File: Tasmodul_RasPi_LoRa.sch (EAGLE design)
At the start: 59 parts, among them J1 691322310002, J2 RASPI_4B, J3 LORA_MPCIE, J4 636101111001, J5 60311002111526, J6 60311002111526, Q1 DMN3404L-7, U1 AP64351, U2 QUECTEL_L76-M33, U3 REG1117

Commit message: * Added more description to the schematic * Added more silk screen information to the PCB * Added U.fl connectors for the SMA connectors as a backup
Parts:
- added J7, J8: 60311002111526, Wurth_Connectors_WR-SMA:60311002111526
- C17, C21: value (none) -> dnp
- J5, J6: value 60311002111526 -> 636101111001; device Wurth_Connectors_WR-SMA:60311002111526 -> Wurth_Connectors_WR-UMRF:636101111001
- R10: value (none) -> 10R
- R11: value (none) -> 0R
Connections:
- new net HF_GNSS: J6.1, J8.1
- new net HF_LORA: J5.1, J7.1
- net GND: now also J7.2, J8.2
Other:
- note added: "GNSS"
- note added: "LoRa"
- note added: "SMA -> U.fl"
- moved on the sheet: J5, J6
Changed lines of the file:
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@@
 <part name="GND20" library="supply1" deviceset="GND" device=""/>
 <part name="L2" library="Wurth_EMC Components_WE-CBF" library_urn="urn:adsk.eagle:library:14283147" deviceset="WE-CBF_0603" device="_WB_HS" package3d_urn="urn:adsk.eagle:package:7784393/8" technology="_74279262" value="120ohm@100 MHz"/>
-<part name="R10" library="rcl" library_urn="urn:adsk.eagle:library:334" deviceset="R-EU_" device="R0603" package3d_urn="urn:adsk.eagle:package:23555/3"/>
+<part name="R10" library="rcl" library_urn="urn:adsk.eagle:library:334" deviceset="R-EU_" device="R0603" package3d_urn="urn:adsk.eagle:package:23555/3" value="10R"/>
 <part name="JMP1" library="jump-0r-smd" library_urn="urn:adsk.eagle:library:251" deviceset="0R-JUMP" device="A" package3d_urn="urn:adsk.eagle:package:15385/1"/>
 <part name="JMP2" library="jump-0r-smd" library_urn="urn:adsk.eagle:library:251" deviceset="0R-JUMP" device="A" package3d_urn="urn:adsk.eagle:package:15385/1"/>
@@
 <part name="D2" library="diode" library_urn="urn:adsk.eagle:library:210" deviceset="DIODE-" device="SOD323-R" package3d_urn="urn:adsk.eagle:package:43437/1" value="CUS551V30,H3F"/>
 <part name="GND22" library="supply1" deviceset="GND" device=""/>
-<part name="J5" library="Wurth_Connectors_WR-SMA" library_urn="urn:adsk.eagle:library:15011170" deviceset="60311002111526" device="" package3d_urn="urn:adsk.eagle:package:15011192/3" value="60311002111526"/>
-<part name="J6" library="Wurth_Connectors_WR-SMA" library_urn="urn:adsk.eagle:library:15011170" deviceset="60311002111526" device="" package3d_urn="urn:adsk.eagle:package:15011192/3" value="60311002111526"/>
-<part name="C17" library="rcl" library_urn="urn:adsk.eagle:library:334" deviceset="C-EU" device="C0603" package3d_urn="urn:adsk.eagle:package:23616/2"/>
-<part name="R11" library="rcl" library_urn="urn:adsk.eagle:library:334" deviceset="R-EU_" device="R0603" package3d_urn="urn:adsk.eagle:package:23555/3"/>
-<part name="C21" library="rcl" library_urn="urn:adsk.eagle:library:334" deviceset="C-EU" device="C0603" package3d_urn="urn:adsk.eagle:package:23616/2"/>
+<part name="J7" library="Wurth_Connectors_WR-SMA" library_urn="urn:adsk.eagle:library:15011170" deviceset="60311002111526" device="" package3d_urn="urn:adsk.eagle:package:15011192/3" value="60311002111526"/>
+<part name="J8" library="Wurth_Connectors_WR-SMA" library_urn="urn:adsk.eagle:library:15011170" deviceset="60311002111526" device="" package3d_urn="urn:adsk.eagle:package:15011192/3" value="60311002111526"/>
+<part name="C17" library="rcl" library_urn="urn:adsk.eagle:library:334" deviceset="C-EU" device="C0603" package3d_urn="urn:adsk.eagle:package:23616/2" value="dnp"/>
+<part name="R11" library="rcl" library_urn="urn:adsk.eagle:library:334" deviceset="R-EU_" device="R0603" package3d_urn="urn:adsk.eagle:package:23555/3" value="0R"/>
+<part name="C21" library="rcl" library_urn="urn:adsk.eagle:library:334" deviceset="C-EU" device="C0603" package3d_urn="urn:adsk.eagle:package:23616/2" value="dnp"/>
+<part name="J5" library="Wurth_Connectors_WR-UMRF" library_urn="urn:adsk.eagle:library:27699748" deviceset="636101111001" device="" package3d_urn="urn:adsk.eagle:package:27699753/5" value="636101111001"/>
+<part name="J6" library="Wurth_Connectors_WR-UMRF" library_urn="urn:adsk.eagle:library:27699748" deviceset="636101111001" device="" package3d_urn="urn:adsk.eagle:package:27699753/5" value="636101111001"/>
 </parts>
 <sheets>
@@
 https://forum.openwrt.org/t/official-raspberry-pi-4-fan-yes-instructions-inside/93975</text>
 <text x="40.64" y="116.84" size="1.778" layer="91" rot="R180">Place only one</text>
+<text x="363.22" y="116.84" size="1.778" layer="91">LoRa</text>
+<text x="363.22" y="101.6" size="1.778" layer="91">GNSS</text>
+<text x="350.52" y="129.54" size="1.778" layer="91" align="center">SMA -&gt; U.fl</text>
 </plain>
 <instances>
@@
 <attribute name="VALUE" x="273.304" y="216.281" size="1.778" layer="96"/>
 </instance>
-<instance part="GND16" gate="1" x="284.48" y="134.62" smashed="yes">
-<attribute name="VALUE" x="281.94" y="132.08" size="1.778" layer="96"/>
+<instance part="GND16" gate="1" x="350.52" y="96.52" smashed="yes">
+<attribute name="VALUE" x="347.98" y="93.98" size="1.778" layer="96"/>
 </instance>
 <instance part="R4" gate="G$1" x="50.8" y="114.3" smashed="yes" rot="MR0">
@@
 <attribute name="VALUE" x="22.86" y="20.32" size="1.778" layer="96"/>
 </instance>
-<instance part="J5" gate="G$1" x="294.64" y="160.02" smashed="yes" rot="MR0">
-<attribute name="NAME" x="294.64" y="163.576" size="1.778" layer="95" rot="MR0" align="bottom-center"/>
-</instance>
-<instance part="J6" gate="G$1" x="294.64" y="144.78" smashed="yes" rot="MR0">
-<attribute name="NAME" x="294.64" y="148.336" size="1.778" layer="95" rot="MR0" align="bottom-center"/>
+<instance part="J7" gate="G$1" x="360.68" y="121.92" smashed="yes" rot="MR0">
+<attribute name="NAME" x="360.68" y="125.476" size="1.778" layer="95" rot="MR0" align="bottom-center"/>
+</instance>
+<instance part="J8" gate="G$1" x="360.68" y="106.68" smashed="yes" rot="MR0">
+<attribute name="NAME" x="360.68" y="110.236" size="1.778" layer="95" rot="MR0" align="bottom-center"/>
 </instance>
 <instance part="C17" gate="G$1" x="228.6" y="66.04" smashed="yes" rot="R180">
@@
 <attribute name="NAME" x="242.316" y="65.659" size="1.778" layer="95" rot="R180"/>
 <attribute name="VALUE" x="242.316" y="70.739" size="1.778" layer="96" rot="R180"/>
+</instance>
+<instance part="J5" gate="G$1" x="337.82" y="121.92" smashed="yes">
+<attribute name="NAME" x="337.82" y="125.476" size="1.778" layer="95" align="bottom-center"/>
+<attribute name="VALUE" x="337.82" y="114.3" size="1.778" layer="96" align="bottom-center"/>
+</instance>
+<instance part="J6" gate="G$1" x="337.82" y="106.68" smashed="yes">
+<attribute name="NAME" x="337.82" y="110.236" size="1.778" layer="95" align="bottom-center"/>
+<attribute name="VALUE" x="337.82" y="99.06" size="1.778" layer="96" align="bottom-center"/>
 </instance>
 </instances>
@@
 </segment>
 <segment>
+<pinref part="J7" gate="G$1" pin="2"/>
+<pinref part="GND16" gate="1" pin="GND"/>
+<wire x1="353.06" y1="116.84" x2="350.52" y2="116.84" width="0.1524" layer="91"/>
+<wire x1="350.52" y1="116.84" x2="350.52" y2="101.6" width="0.1524" layer="91"/>
+<pinref part="J8" gate="G$1" pin="2"/>
+<wire x1="350.52" y1="101.6" x2="350.52" y2="99.06" width="0.1524" layer="91"/>
+<wire x1="353.06" y1="101.6" x2="350.52" y2="101.6" width="0.1524" layer="91"/>
+<junction x="350.52" y="101.6"/>
 <pinref part="J5" gate="G$1" pin="2"/>
-<pinref part="GND16" gate="1" pin="GND"/>
-<wire x1="287.02" y1="154.94" x2="284.48" y2="154.94" width="0.1524" layer="91"/>
-<wire x1="284.48" y1="154.94" x2="284.48" y2="139.7" width="0.1524" layer="91"/>
+<wire x1="345.44" y1="116.84" x2="350.52" y2="116.84" width="0.1524" layer="91"/>
+<junction x="350.52" y="116.84"/>
 <pinref part="J6" gate="G$1" pin="2"/>
-<wire x1="284.48" y1="139.7" x2="284.48" y2="137.16" width="0.1524" layer="91"/>
-<wire x1="287.02" y1="139.7" x2="284.48" y2="139.7" width="0.1524" layer="91"/>
-<junction x="284.48" y="139.7"/>
+<wire x1="345.44" y1="101.6" x2="350.52" y2="101.6" width="0.1524" layer="91"/>
 </segment>
 <segment>
@@
 </segment>
 </net>
+<net name="HF_LORA" class="1">
+<segment>
+<pinref part="J5" gate="G$1" pin="1"/>
+<pinref part="J7" gate="G$1" pin="1"/>
+<wire x1="345.44" y1="121.92" x2="353.06" y2="121.92" width="0.1524" layer="91"/>
+</segment>
+</net>
+<net name="HF_GNSS" class="1">
+<segment>
+<pinref part="J6" gate="G$1" pin="1"/>
+<pinref part="J8" gate="G$1" pin="1"/>
+<wire x1="345.44" y1="106.68" x2="353.06" y2="106.68" width="0.1524" layer="91"/>
+</segment>
+</net>

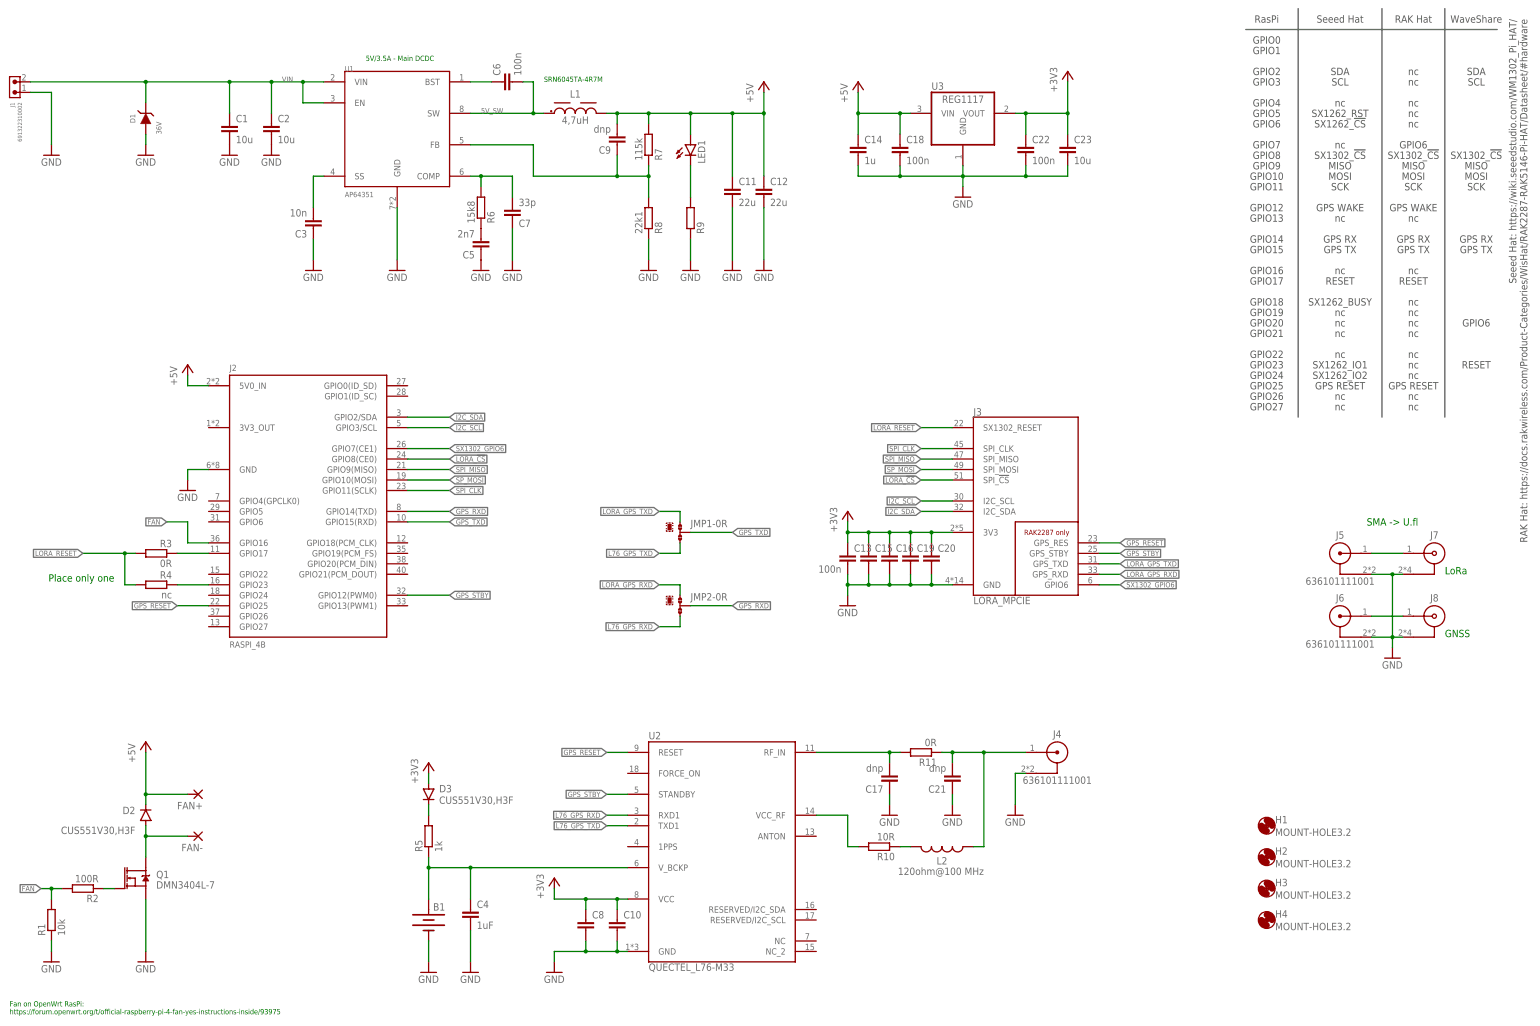
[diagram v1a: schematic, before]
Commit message: * Added multifuse to power input * Added I2C pullup resistors * Added test points to unused GPS module pins * Updated README.md
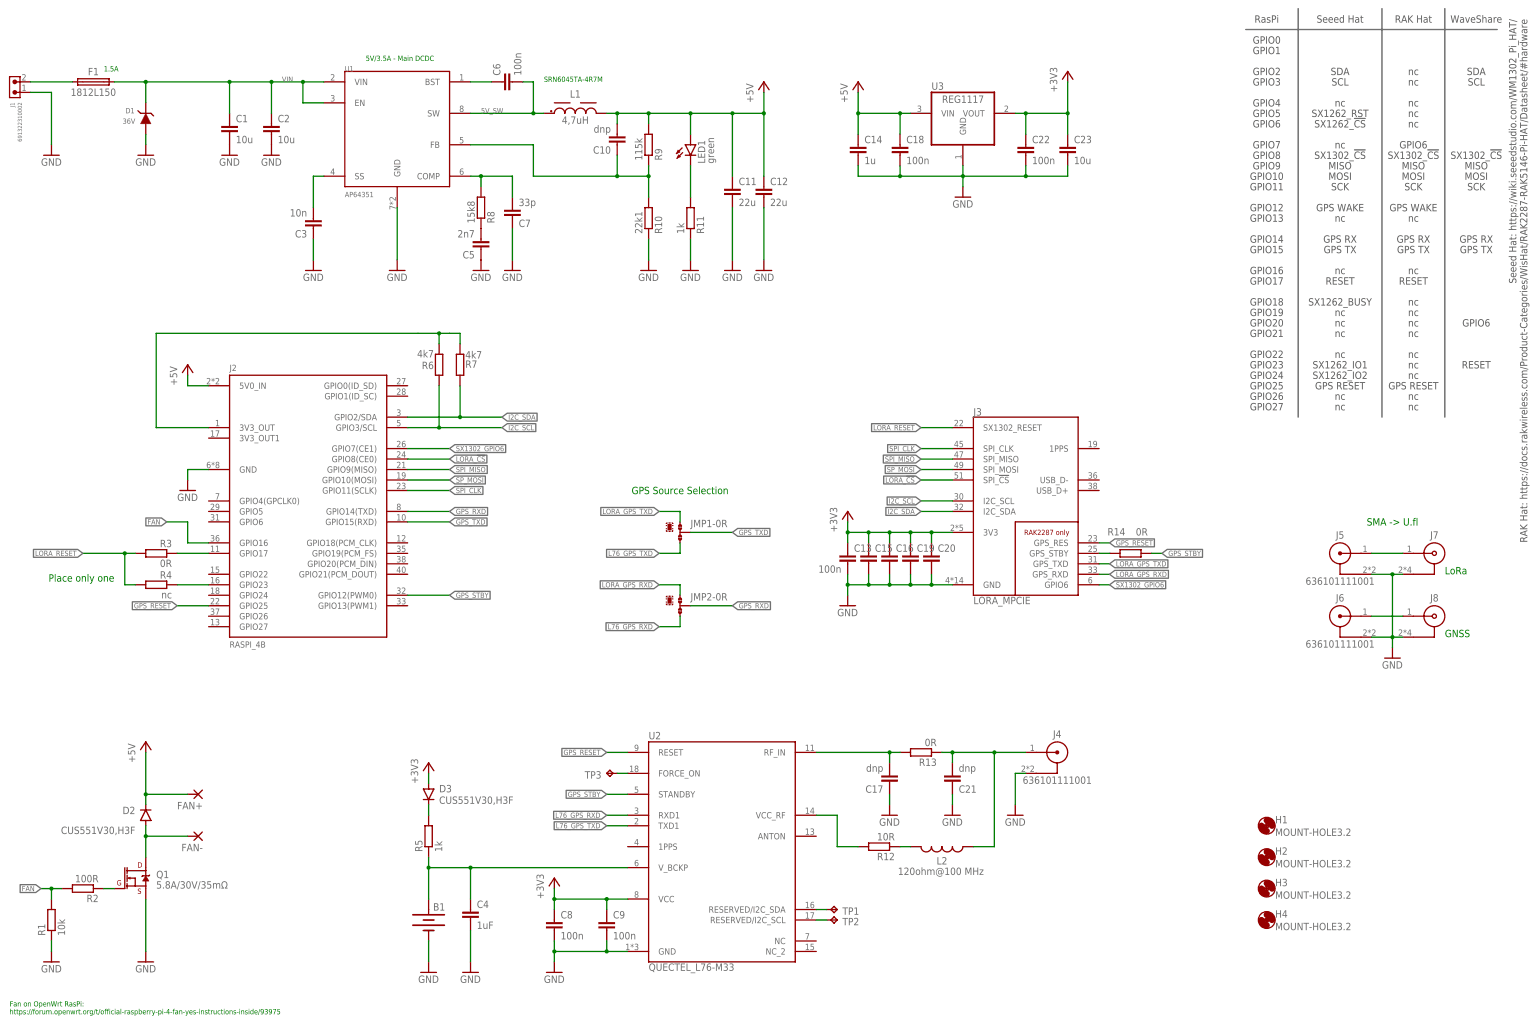
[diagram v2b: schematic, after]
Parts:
- added F1: 1812L150, Fuse:1812L150
- added R12: 10R, rcl:R-EU_R0603
- added R13, R14: 0R, rcl:R-EU_R0603
- added TP1, TP2, TP3: TPTP15R, testpad:TPTP15R
- C10: value (none) -> dnp
- C15, C16, C19, C20, C8: value (none) -> 100n
- C9: value dnp -> 100n
- LED1: value (none) -> green
- Q1: value DMN3404L-7 -> 5.8A/30V/35mΩ
- R10: value 10R -> 22k1
- R11: value 0R -> 1k
- R6: value 15k8 -> 4k7
- R7: value 115k -> 4k7
- R8: value 22k1 -> 15k8
- R9: value (none) -> 115k
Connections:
- new net N$13: J2.3V3_OUT, R6.2, R7.2
- new net N$15: F1.1, J1.2
- new net N$16: TP1.TP, U2.RESERVED/I2C_SDA
- new net N$17: TP2.TP, U2.RESERVED/I2C_SCL
- new net N$18: TP3.TP, U2.FORCE_ON
- new net N$19: J3.GPS_STBY, R14.2
- net +3V3: now also C9.1; no longer C10.1
- net +5V: now also C10.2, R9.2; no longer C9.2, R7.2
- net GND: now also C9.2, R10.1, R11.1; no longer C10.2, R8.1, R9.1
- net GPS_STBY: now also R14.1; no longer J3.GPS_STBY
- net I2C_SCL: now also R6.1
- net I2C_SDA: now also R7.1
- net N$10: now also R12.2; no longer R10.2
- net N$11: now also R8.1; no longer R6.1
- net N$12: now also R8.2; no longer R6.2
- net N$4: now also R12.1; no longer R10.1
- net N$6: now also C10.1, R10.2, R9.1; no longer C9.1, R7.1, R8.2
- net N$7: now also R11.2; no longer R9.2
- net RF_CON: now also R13.1; no longer R11.1
- net RF_MATCHED: now also R13.2; no longer R11.2
- net VIN: now also F1.2; no longer J1.2
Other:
- note added: "1.5A"
- note added: "GPS Source Selection"
- moved on the sheet: C10, C8, C9, R10, R11, R6, R7, R8, R9

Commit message: * Added 3 status LEDs to the RasPi * Minor Layout tweaks
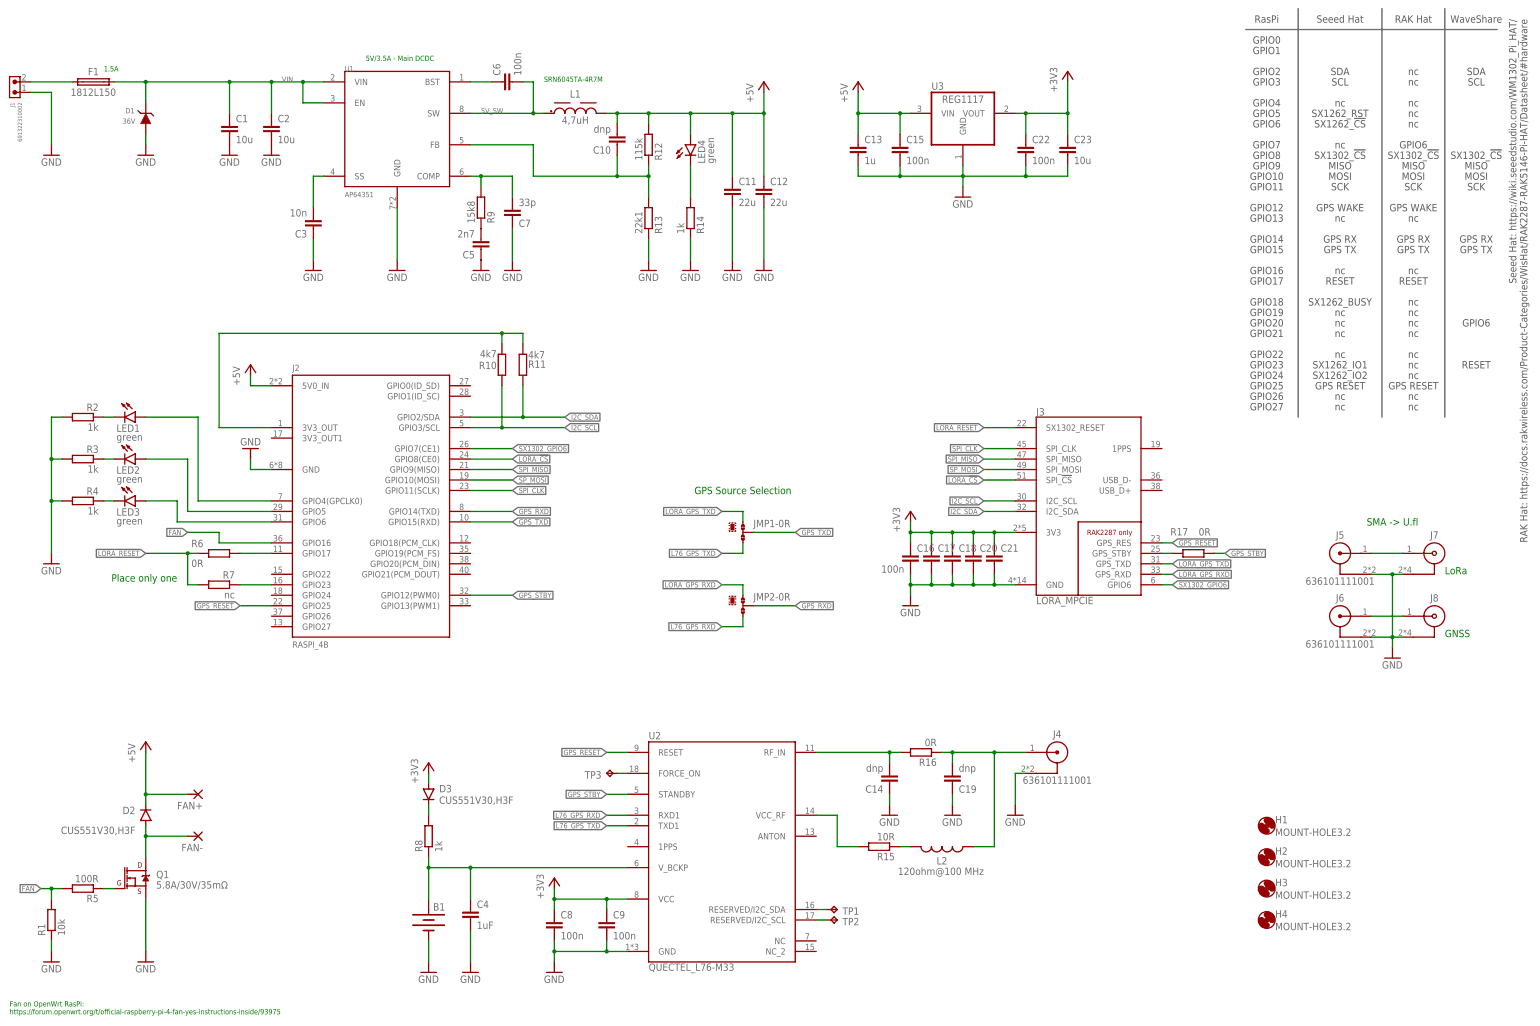
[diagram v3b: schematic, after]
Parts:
- added LED2, LED3, LED4: green, led:LEDCHIPLED_0603
- added R15: 10R, rcl:R-EU_R0603
- added R16, R17: 0R, rcl:R-EU_R0603
- C13: value 100n -> 1u
- C14: value 1u -> dnp
- C17, C21: value dnp -> 100n
- C19: value 100n -> dnp
- R10: value 22k1 -> 4k7
- R11: value 1k -> 4k7
- R12: value 10R -> 115k
- R13: value 0R -> 22k1
- R14, R3: value 0R -> 1k
- R2: value 100R -> 1k
- R4: value nc -> 1k
- R5: value 1k -> 100R
- R6: value 4k7 -> 0R
- R7: value 4k7 -> nc
- R8: value 15k8 -> 1k
- R9: value 115k -> 15k8
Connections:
- new net N$20: LED1.C, R2.1
- new net N$21: LED2.C, R3.1
- new net N$22: LED3.C, R4.1
- new net N$23: J2.GPIO4(GPCLK0), LED1.A
- new net N$24: J2.GPIO5, LED2.A
- new net N$25: J2.GPIO6, LED3.A
- net +3V3: now also C17.1, C18.1, C21.1; no longer C13.1, C15.1, C19.1
- net +5V: now also C13.1, C15.1, LED4.A, R12.2; no longer C14.1, C18.1, LED1.A, R9.2
- net FAN: now also R5.2; no longer R2.2
- net GND: now also C14.1, C17.2, C19.1, C21.2, R13.1, R14.1, R2.2, R3.2, R4.2; no longer C14.2, C17.1, C19.2, C21.1, R10.1, R11.1
- net GPS_STBY: now also R17.1; no longer R14.1
- net I2C_SCL: now also R10.1; no longer R6.1
- net I2C_SDA: now also R11.1; no longer R7.1
- net LORA_RESET: now also R6.2, R7.2; no longer R3.2, R4.2
- net N$1: now also R7.1; no longer R4.1
- net N$10: now also R15.2; no longer R12.2
- net N$11: now also R9.1; no longer R8.1
- net N$12: now also R9.2; no longer R8.2
- net N$13: now also R10.2, R11.2; no longer R6.2, R7.2
- net N$19: now also R17.2; no longer R14.2
- net N$3: now also R6.1; no longer R3.1
- net N$4: now also R15.1; no longer R12.1
- net N$6: now also R12.1, R13.2; no longer R10.2, R9.1
- net N$7: now also LED4.C, R14.2; no longer LED1.C, R11.2
- net N$8: now also R8.2; no longer R5.2
- net N$9: now also R5.1; no longer R2.1
- net RF_CON: now also C19.2, R16.1; no longer C21.2, R13.1
- net RF_MATCHED: now also C14.2, R16.2; no longer C17.2, R13.2
- net VBAT: now also R8.1; no longer R5.1
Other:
- moved on the sheet: C13, C14, C15, C16, C17, C18, C19, C20, C21, J2, J3, JMP1-0R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
